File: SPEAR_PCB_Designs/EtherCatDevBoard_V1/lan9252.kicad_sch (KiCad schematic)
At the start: 29 parts, among them U4 LAN9252I/ML, Y2 25MHz

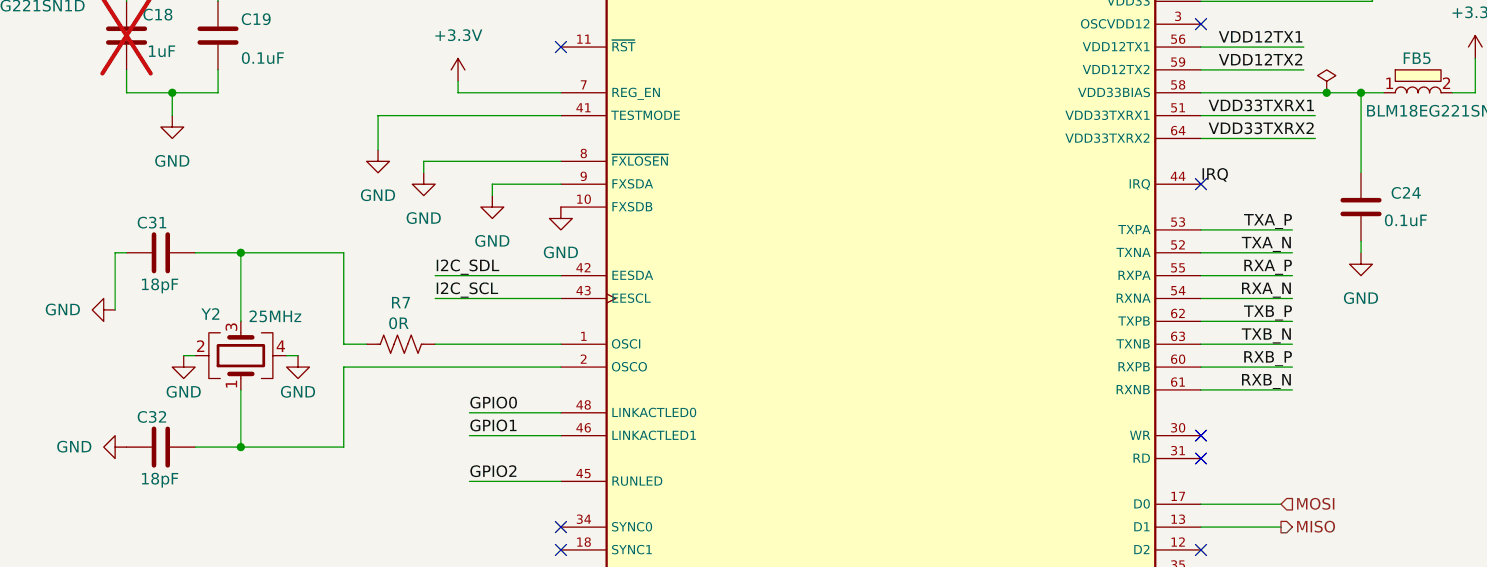
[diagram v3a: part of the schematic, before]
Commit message: Continued work on EtherCAT microcontroller dev board. Updated it's head pinout.
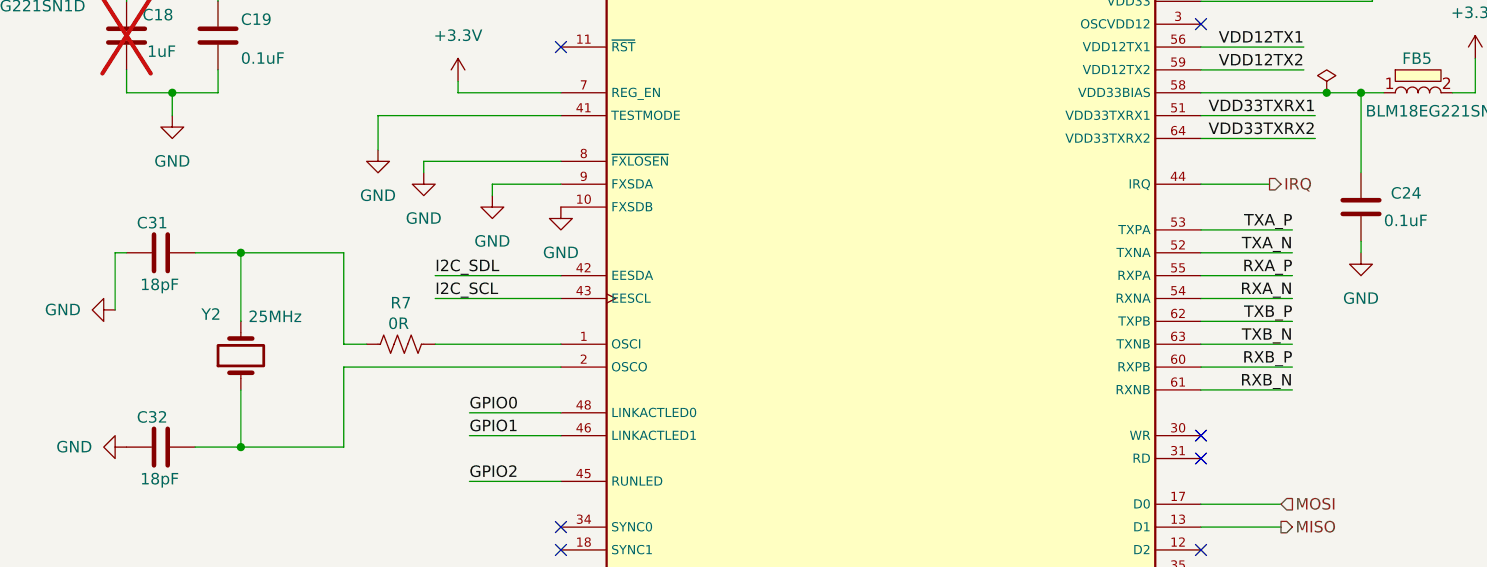
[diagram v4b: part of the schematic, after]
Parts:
- Y2: footprint Crystal:Crystal_SMD_Abracon_ABM8G-4Pin_3.2x2.5mm -> LAN9252 Footprints:Y_Wurth_WE-XTAL_Quartz-HC49-4HSMX; symbol Device:Crystal_GND24 -> Device:Crystal
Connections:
- net GND: no longer Y2.2, Y2.4
- net at C31.2, R7.1: now also Y2.2; no longer Y2.3
- no-connect marks 24 -> 23
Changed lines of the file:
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@@
 	)
 	(no_connect
-		(at 156.21 69.85)
-	)
-	(no_connect
 		(at 85.09 128.27)
 	)
@@
 	(wire
 		(pts
-			(xy 43.18 88.9) (xy 44.45 88.9)
-		)
-		(stroke
-			(width 0)
-			(type default)
-		)
-	)
-	(wire
-		(pts
 			(xy 41.91 59.69) (xy 46.99 59.69)
 		)
@@
 	(wire
 		(pts
-			(xy 55.88 88.9) (xy 54.61 88.9)
-		)
-		(stroke
-			(width 0)
-			(type default)
-		)
-	)
-	(wire
-		(pts
 			(xy 215.9 55.88) (xy 215.9 59.69)
 		)
@@
 	(wire
 		(pts
+			(xy 163.83 69.85) (xy 156.21 69.85)
+		)
+		(stroke
+			(width 0)
+			(type default)
+		)
+	)
+	(wire
+		(pts
 			(xy 19.05 45.72) (xy 19.05 48.26)
 		)
@@
 		)
 	)
-	(label "IRQ"
-		(at 156.21 69.85 0)
-		(effects
-			(font
-				(size 1.27 1.27)
-			)
-			(justify left bottom)
-		)
-	)
 	(label "I2C_SDL"
 		(at 213.36 149.86 0)
@@
 		)
 	)
+	(hierarchical_label "IRQ"
+		(shape output)
+		(at 163.83 69.85 0)
+		(effects
+			(font
+				(size 1.27 1.27)
+			)
+			(justify left)
+		)
+	)
 	(hierarchical_label "MOSI"
 		(shape input)
@@
 	)
 	(symbol
-		(lib_id "power:GND")
-		(at 55.88 88.9 0)
-		(unit 1)
-		(exclude_from_sim no)
-		(in_bom yes)
-		(on_board yes)
-		(dnp no)
-		(property "Reference" "#PWR070"
-			(at 55.88 95.25 0)
-			(effects
-				(font
-					(size 1.27 1.27)
-				)
-				(hide yes)
-			)
-		)
-		(property "Value" "GND"
-			(at 55.88 92.964 0)
-			(effects
-				(font
-					(size 1.27 1.27)
-				)
-			)
-		)
-		(property "Footprint" ""
-			(at 55.88 88.9 0)
-			(effects
-				(font
-					(size 1.27 1.27)
-				)
-				(hide yes)
-			)
-		)
-		(property "Datasheet" ""
-			(at 55.88 88.9 0)
-			(effects
-				(font
-					(size 1.27 1.27)
-				)
-				(hide yes)
-			)
-		)
-		(property "Description" "Power symbol creates a global label with name \"GND\" , ground"
-			(at 55.88 88.9 0)
-			(effects
-				(font
-					(size 1.27 1.27)
-				)
-				(hide yes)
-			)
-		)
-		(pin "1"
-		)
-		(instances
-			(project "SPEAR_V1"
-				(path "/6af343d7-7346-4b6a-90ee-eb113982f4e5/d630782a-bbb8-450e-a52a-35375a587c4e"
-					(reference "#PWR070")
-					(unit 1)
-				)
-			)
-		)
-	)
-	(symbol
 		(lib_id "Device:C")
 		(at 223.52 63.5 0)
@@
 	)
 	(symbol
-		(lib_id "Device:Crystal_GND24")
+		(lib_id "Device:Crystal")
 		(at 49.53 88.9 90)
 		(unit 1)
@@
 			)
 		)
-		(property "Footprint" "Crystal:Crystal_SMD_Abracon_ABM8G-4Pin_3.2x2.5mm"
+		(property "Footprint" "LAN9252 Footprints:Y_Wurth_WE-XTAL_Quartz-HC49-4HSMX"
 			(at 49.53 88.9 0)
 			(effects
@@
 			)
 		)
-		(property "Description" "Four pin crystal, GND on pins 2 and 4"
+		(property "Description" "Two pin crystal"
 			(at 49.53 88.9 0)
 			(effects
@@
 		(pin "2"
 		)
-		(pin "3"
-		)
-		(pin "4"
-		)
 		(instances
 			(project "SPEAR_V1"
@@
 					(unit 1)
 				)
-			)
-		)
-	)
-	(symbol
-		(lib_id "power:GND")
-		(at 43.18 88.9 0)
-		(unit 1)
-		(exclude_from_sim no)
-		(in_bom yes)
-		(on_board yes)
-		(dnp no)
-		(property "Reference" "#PWR069"
-			(at 43.18 95.25 0)
-			(effects
-				(font
-					(size 1.27 1.27)
-				)
-				(hide yes)
-			)
-		)
-		(property "Value" "GND"
-			(at 43.18 92.964 0)
-			(effects
-				(font
-					(size 1.27 1.27)
-				)
-			)
-		)
-		(property "Footprint" ""
-			(at 43.18 88.9 0)
-			(effects
-				(font
-					(size 1.27 1.27)
-				)
-				(hide yes)
-			)
-		)
-		(property "Datasheet" ""
-			(at 43.18 88.9 0)
-			(effects
-				(font
-					(size 1.27 1.27)
-				)
-				(hide yes)
-			)
-		)
-		(property "Description" "Power symbol creates a global label with name \"GND\" , ground"
-			(at 43.18 88.9 0)
-			(effects
-				(font
-					(size 1.27 1.27)
-				)
-				(hide yes)
-			)
-		)
-		(pin "1"
-		)
-		(instances
-			(project "SPEAR_V1"
-				(path "/6af343d7-7346-4b6a-90ee-eb113982f4e5/d630782a-bbb8-450e-a52a-35375a587c4e"
-					(reference "#PWR069")
-					(unit 1)
-				)

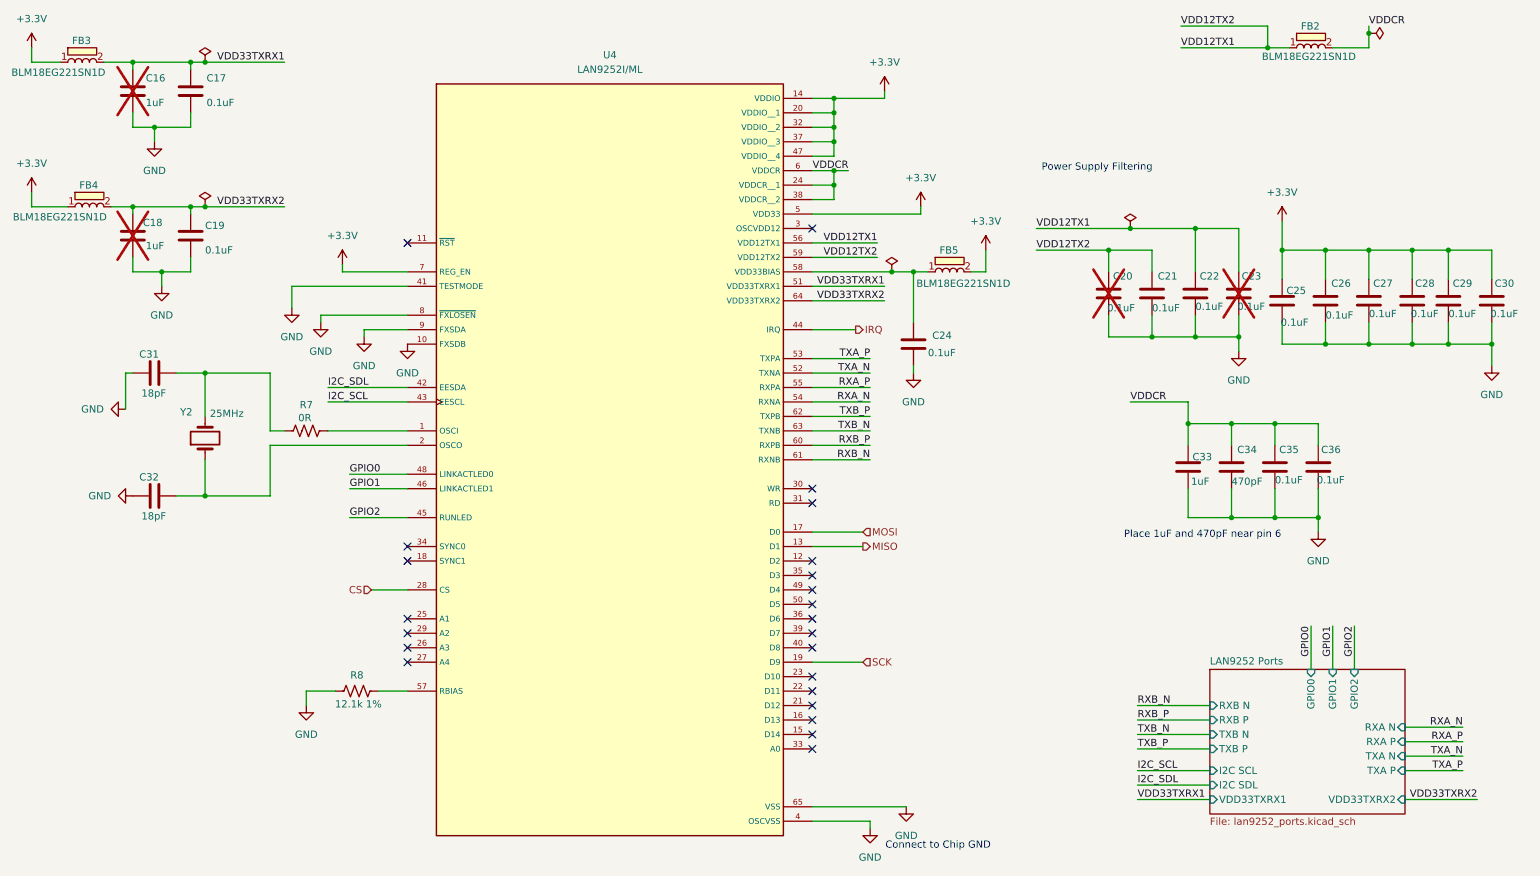
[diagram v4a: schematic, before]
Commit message: Started adding digikey part ID's to the EtherCAT microcontroller dev. board, but incomplete as of now.
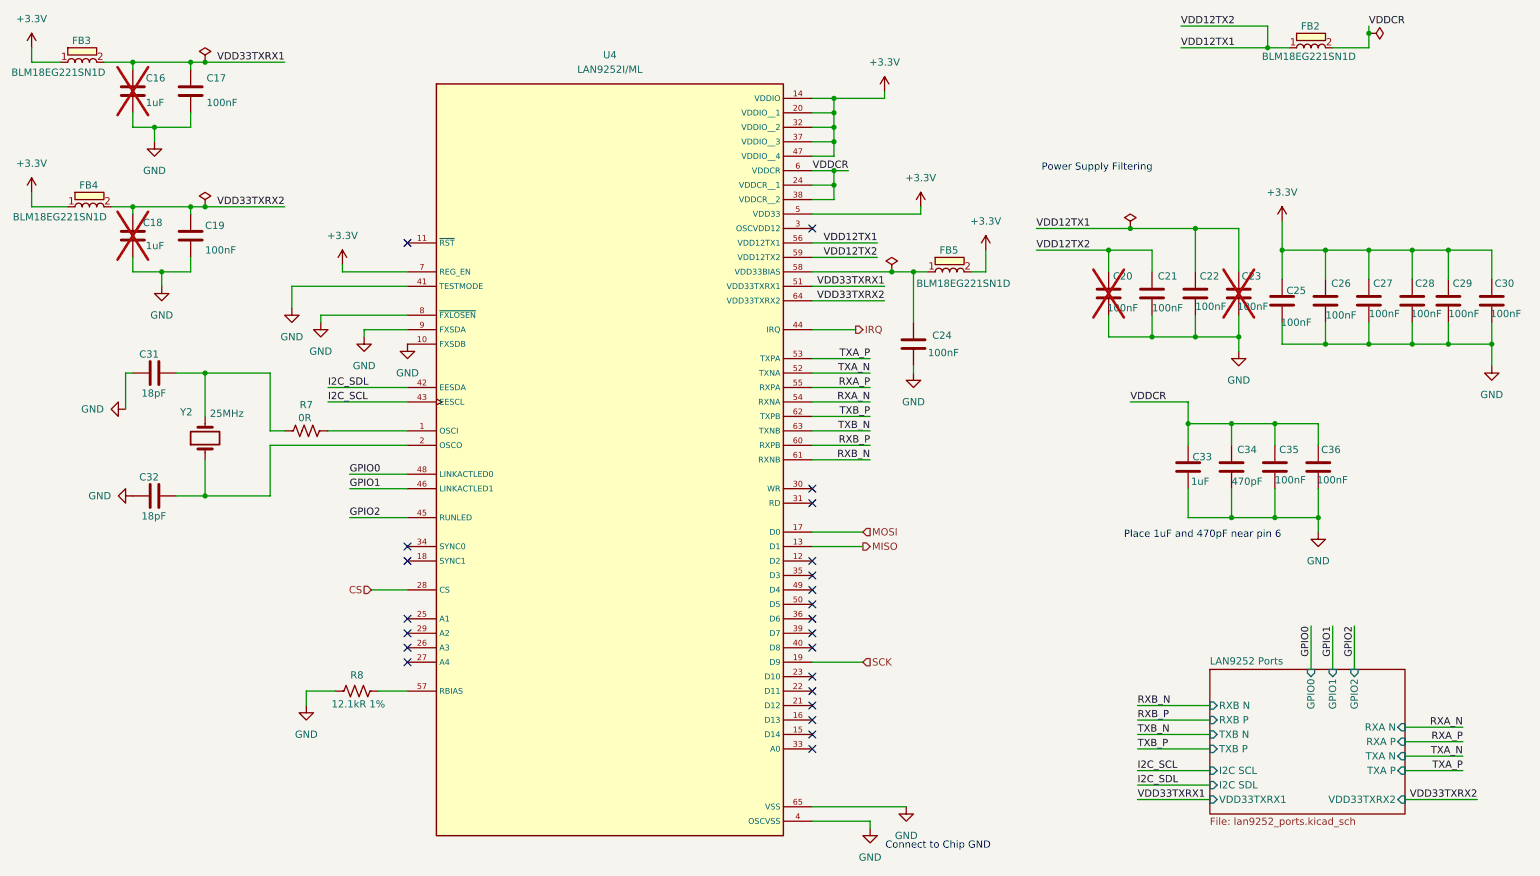
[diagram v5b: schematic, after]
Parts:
- C16, C18, C33: DigiKey_Part_Number (none) -> 1276-1067-1-ND
- C17, C19, C20, C21, C22, C23, C24, C25, C26, C27, C28, C29, C30, C35, C36: value 0.1uF -> 100nF; DigiKey_Part_Number (none) -> 1276-1043-1-ND
- C31, C32: DigiKey_Part_Number (none) -> 1276-6612-1-ND
- C34: DigiKey_Part_Number (none) -> 1276-1566-1-ND
- R7: DigiKey_Part_Number (none) -> 311-0.0JRCT-ND
- R8: value 12.1k 1% -> 12.1kR 1%; DigiKey_Part_Number (none) -> 311-12.1KLRCT-ND
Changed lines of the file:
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@@
 			)
 		)
-		(property "Value" "0.1uF"
+		(property "Value" "100nF"
 			(at 208.026 66.04 0)
 			(effects
@@
 			)
 		)
+		(property "DigiKey_Part_Number" "1276-1043-1-ND"
+			(at 208.28 63.5 0)
+			(effects
+				(font
+					(size 1.27 1.27)
+				)
+				(hide yes)
+			)
+		)
 		(pin "2"
 		)
@@
 			)
 		)
-		(property "Value" "0.1uF"
+		(property "Value" "100nF"
 			(at 215.9 66.04 0)
 			(effects
@@
 			)
 		)
+		(property "DigiKey_Part_Number" "1276-1043-1-ND"
+			(at 215.9 63.5 0)
+			(effects
+				(font
+					(size 1.27 1.27)
+				)
+				(hide yes)
+			)
+		)
 		(pin "2"
 		)
@@
 			)
 		)
-		(property "Value" "0.1uF"
+		(property "Value" "100nF"
 			(at 246.38 67.31 0)
 			(effects
@@
 			)
 		)
+		(property "DigiKey_Part_Number" "1276-1043-1-ND"
+			(at 246.38 64.77 0)
+			(effects
+				(font
+					(size 1.27 1.27)
+				)
+				(hide yes)
+			)
+		)
 		(pin "2"
 		)
@@
 			)
 		)
-		(property "Value" "0.1uF"
+		(property "Value" "100nF"
 			(at 223.52 65.786 0)
 			(effects
@@
 			)
 		)
+		(property "DigiKey_Part_Number" "1276-1043-1-ND"
+			(at 223.52 63.5 0)
+			(effects
+				(font
+					(size 1.27 1.27)
+				)
+				(hide yes)
+			)
+		)
 		(pin "2"
 		)
@@
 			)
 		)
+		(property "DigiKey_Part_Number" "1276-1067-1-ND"
+			(at 222.25 93.98 0)
+			(effects
+				(font
+					(size 1.27 1.27)
+				)
+				(hide yes)
+			)
+		)
 		(pin "2"
 		)
@@
 			)
 		)
+		(property "DigiKey_Part_Number" "1276-6612-1-ND"
+			(at 40.64 77.47 90)
+			(effects
+				(font
+					(size 1.27 1.27)
+				)
+				(hide yes)
+			)
+		)
 		(pin "1"
 		)
@@
 			)
 		)
-		(property "Value" "0.1uF"
+		(property "Value" "100nF"
 			(at 176.53 73.914 0)
 			(effects
@@
 			)
 		)
+		(property "DigiKey_Part_Number" "1276-1043-1-ND"
+			(at 173.99 72.39 0)
+			(effects
+				(font
+					(size 1.27 1.27)
+				)
+				(hide yes)
+			)
+		)
 		(pin "2"
 		)
@@
 			)
 		)
-		(property "Value" "0.1uF"
+		(property "Value" "100nF"
 			(at 261.366 67.056 0)
 			(effects
@@
 			)
 		)
+		(property "DigiKey_Part_Number" "1276-1043-1-ND"
+			(at 261.62 64.77 0)
+			(effects
+				(font
+					(size 1.27 1.27)
+				)
+				(hide yes)
+			)
+		)
 		(pin "2"
 		)
@@
 			)
 		)
-		(property "Value" "0.1uF"
+		(property "Value" "100nF"
 			(at 244.856 96.266 0)
 			(effects
@@
 			)
 		)
+		(property "DigiKey_Part_Number" "1276-1043-1-ND"
+			(at 245.11 93.98 0)
+			(effects
+				(font
+					(size 1.27 1.27)
+				)
+				(hide yes)
+			)
+		)
 		(pin "2"
 		)
@@
 			)
 		)
-		(property "Value" "0.1uF"
+		(property "Value" "100nF"
 			(at 230.886 65.786 0)
 			(effects
@@
 			)
 		)
+		(property "DigiKey_Part_Number" "1276-1043-1-ND"
+			(at 231.14 63.5 0)
+			(effects
+				(font
+					(size 1.27 1.27)
+				)
+				(hide yes)
+			)
+		)
 		(pin "2"
 		)
@@
 			)
 		)
-		(property "Value" "0.1uF"
+		(property "Value" "100nF"
 			(at 237.49 96.266 0)
 			(effects
@@
 			)
 		)
+		(property "DigiKey_Part_Number" "1276-1043-1-ND"
+			(at 237.49 93.98 0)
+			(effects
+				(font
+					(size 1.27 1.27)
+				)
+				(hide yes)
+			)
+		)
 		(pin "2"
 		)
@@
 			)
 		)
-		(property "Value" "12.1k 1%"
+		(property "Value" "12.1kR 1%"
 			(at 76.454 135.636 90)
 			(effects
@@
 			)
 		)
+		(property "DigiKey_Part_Number" "311-12.1KLRCT-ND"
+			(at 76.2 133.35 90)
+			(effects
+				(font
+					(size 1.27 1.27)
+				)
+				(hide yes)
+			)
+		)
 		(pin "1"
 		)
@@
 			)
 		)
-		(property "Value" "0.1uF"
+		(property "Value" "100nF"
 			(at 254 67.056 0)
 			(effects
@@
 			)
 		)
+		(property "DigiKey_Part_Number" "1276-1043-1-ND"
+			(at 254 64.77 0)
+			(effects
+				(font
+					(size 1.27 1.27)
+				)
+				(hide yes)
+			)
+		)
 		(pin "2"
 		)
@@
 			)
 		)
-		(property "Value" "0.1uF"
+		(property "Value" "100nF"
 			(at 275.336 67.056 0)
 			(effects
@@
 			)
 		)
+		(property "DigiKey_Part_Number" "1276-1043-1-ND"
+			(at 275.59 64.77 0)
+			(effects
+				(font
+					(size 1.27 1.27)
+				)
+				(hide yes)
+			)
+		)
 		(pin "2"
 		)
@@
 			)
 		)
-		(property "Value" "0.1uF"
+		(property "Value" "100nF"
 			(at 49.784 29.972 0)
 			(effects
@@
 			)
 		)
+		(property "DigiKey_Part_Number" "1276-1043-1-ND"
+			(at 46.99 27.94 0)
+			(effects
+				(font
+					(size 1.27 1.27)
+				)
+				(hide yes)
+			)
+		)
 		(pin "2"
 		)
@@
 			)
 		)
+		(property "DigiKey_Part_Number" "1276-6612-1-ND"
+			(at 40.64 99.06 90)
+			(effects
+				(font
+					(size 1.27 1.27)
+				)
+				(hide yes)
+			)
+		)
 		(pin "1"
 		)
@@
 			)
 		)
-		(property "Value" "0.1uF"
+		(property "Value" "100nF"
 			(at 49.53 55.88 0)
 			(effects
@@
 			)
 		)
+		(property "DigiKey_Part_Number" "1276-1043-1-ND"
+			(at 46.99 53.34 0)
+			(effects
+				(font
+					(size 1.27 1.27)
+				)
+				(hide yes)
+			)
+		)
 		(pin "2"
 		)
@@
 			)
 		)
+		(property "DigiKey_Part_Number" "311-0.0JRCT-ND"
+			(at 67.31 87.63 90)
+			(effects
+				(font
+					(size 1.27 1.27)
+				)
+				(hide yes)
+			)
+		)
 		(pin "1"
 		)
@@
 			)
 		)
+		(property "DigiKey_Part_Number" "1276-1067-1-ND"
+			(at 36.83 53.34 0)
+			(effects
+				(font
+					(size 1.27 1.27)
+				)
+				(hide yes)
+			)
+		)
 		(pin "1"
 		)
@@
 			)
 		)
+		(property "DigiKey_Part_Number" "1276-1566-1-ND"
+			(at 229.87 93.98 0)
+			(effects
+				(font
+					(size 1.27 1.27)
+				)
+				(hide yes)
+			)
+		)
 		(pin "2"
 		)
@@
 			)
 		)
-		(property "Value" "0.1uF"
+		(property "Value" "100nF"
 			(at 238.506 68.58 0)
 			(effects
@@
 			)
 		)
+		(property "DigiKey_Part_Number" "1276-1043-1-ND"
+			(at 238.76 64.77 0)
+			(effects
+				(font
+					(size 1.27 1.27)
+				)
+				(hide yes)
+			)
+		)
 		(pin "2"
 		)
@@
 			)
 		)
-		(property "Value" "0.1uF"
+		(property "Value" "100nF"
 			(at 267.97 67.056 0)
 			(effects
@@
 			)
 		)
+		(property "DigiKey_Part_Number" "1276-1043-1-ND"
+			(at 267.97 64.77 0)
+			(effects
+				(font
+					(size 1.27 1.27)
+				)
+				(hide yes)
+			)
+		)
 		(pin "2"
 		)
@@
 			(at 36.83 27.94 0)
 			(effects
+				(font
+					(size 1.27 1.27)
+				)
+				(hide yes)
+			)
+		)
+		(property "DigiKey_Part_Number" "1276-1067-1-ND"
+			(at 36.83 27.94 0)
+			(effects

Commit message: Finished etherCAT microcontroller dev board component selection. BOM is available. PCB layout incomplete.
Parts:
- FB2, FB3, FB4, FB5: DigiKey_Part_Number (none) -> 490-3992-1-ND
- U4: DigiKey_Part_Number (none) -> LAN9252I/ML-ND
- Y2: DigiKey_Part_Number (none) -> 732-830056463CT-ND
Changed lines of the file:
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@@
 			)
 		)
+		(property "DigiKey_Part_Number" "490-3992-1-ND"
+			(at 180.34 59.69 0)
+			(effects
+				(font
+					(size 1.27 1.27)
+				)
+				(hide yes)
+			)
+		)
 		(pin "2"
 		)
@@
 			)
 		)
+		(property "DigiKey_Part_Number" "732-830056463CT-ND"
+			(at 49.53 88.9 90)
+			(effects
+				(font
+					(size 1.27 1.27)
+				)
+				(hide yes)
+			)
+		)
 		(pin "1"
 		)
@@
 			)
 		)
+		(property "DigiKey_Part_Number" "LAN9252I/ML-ND"
+			(at 121.92 88.9 0)
+			(effects
+				(font
+					(size 1.27 1.27)
+				)
+				(hide yes)
+			)
+		)
 		(pin "58"
 		)
@@
 			)
 		)
+		(property "DigiKey_Part_Number" "490-3992-1-ND"
+			(at 29.21 48.26 0)
+			(effects
+				(font
+					(size 1.27 1.27)
+				)
+				(hide yes)
+			)
+		)
 		(pin "2"
 		)
@@
 			)
 		)
+		(property "DigiKey_Part_Number" "490-3992-1-ND"
+			(at 27.94 22.86 0)
+			(effects
+				(font
+					(size 1.27 1.27)
+				)
+				(hide yes)
+			)
+		)
 		(pin "2"
 		)
@@
 			(at 243.84 20.32 0)
 			(effects
+				(font
+					(size 1.27 1.27)
+				)
+				(hide yes)
+			)
+		)
+		(property "DigiKey_Part_Number" "490-3992-1-ND"
+			(at 243.84 20.32 0)
+			(effects
